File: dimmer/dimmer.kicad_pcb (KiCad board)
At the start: 2 copper layers, 16 parts, among them J1 Conn_01x04, J2 Conn_01x04, Q1 TIC216, U1 4N25, U2 MOC3021M

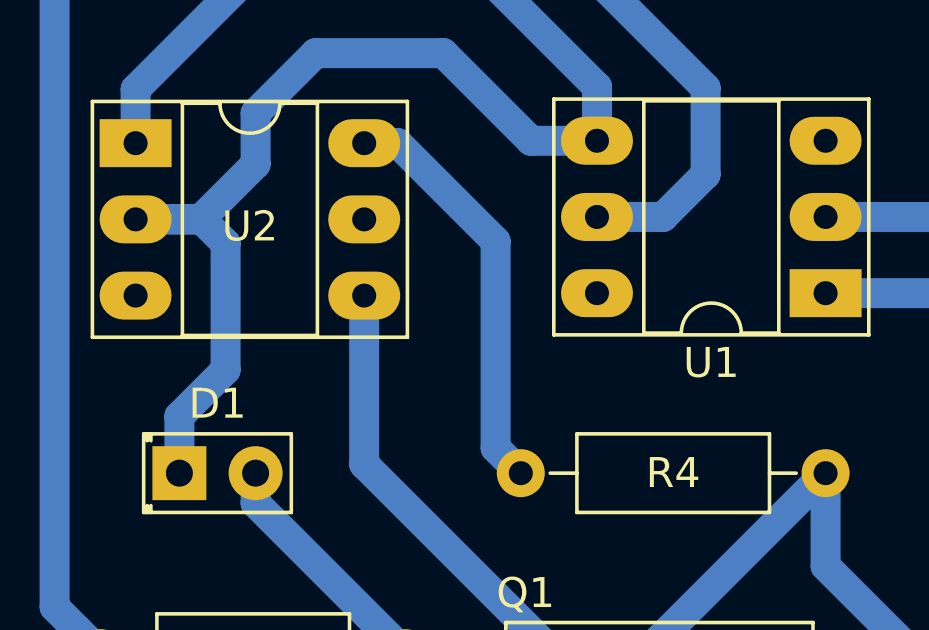
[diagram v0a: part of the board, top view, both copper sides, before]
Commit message: update resistences 1W values
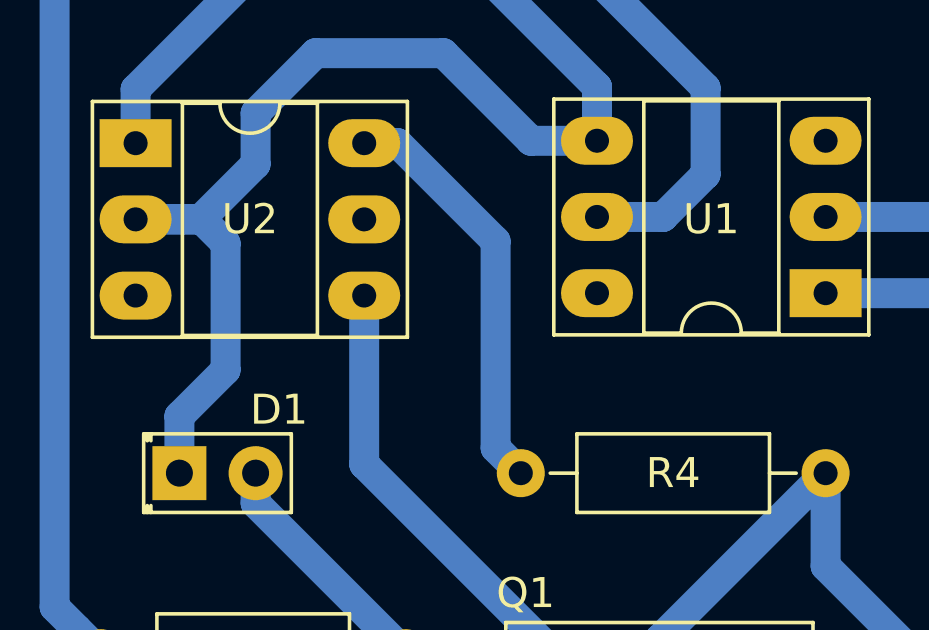
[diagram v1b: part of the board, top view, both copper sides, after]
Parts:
- R5, R6: value 30k/1W -> 15k/1W
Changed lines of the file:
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@@
     (visible_elements FFFFFF7F)
     (pcbplotparams
-      (layerselection 0x010fc_ffffffff)
+      (layerselection 0x3ffff_ffffffff)
       (usegerberextensions false)
       (usegerberattributes false)
@@
       (excludeedgelayer true)
       (linewidth 0.100000)
-      (plotframeref false)
+      (plotframeref true)
       (viasonmask false)
       (mode 1)
@@
       (padsonsilk false)
       (subtractmaskfromsilk false)
-      (outputformat 1)
-      (mirror false)
-      (drillshape 1)
+      (outputformat 4)
+      (mirror true)
+      (drillshape 0)
       (scaleselection 1)
-      (outputdirectory ""))
+      (outputdirectory "plot/"))
   )
   (net 0 "")
@@
     (descr "6-lead though-hole mounted DIP package, row spacing 7.62 mm (300 mils), Socket, LongPads")
     (tags "THT DIP DIL PDIP 2.54mm 7.62mm 300mil Socket LongPads")
-    (fp_text reference U2 (at 3.81 2.78) (layer F.SilkS)
+    (fp_text reference U2 (at 3.81 2.538) (layer F.SilkS)
       (effects (font (size 1 1) (thickness 0.15)))
     )
@@
     (descr "6-lead though-hole mounted DIP package, row spacing 7.62 mm (300 mils), Socket, LongPads")
     (tags "THT DIP DIL PDIP 2.54mm 7.62mm 300mil Socket LongPads")
-    (fp_text reference U1 (at 3.81 -2.33 180) (layer F.SilkS)
+    (fp_text reference U1 (at 3.81 2.462 180) (layer F.SilkS)
       (effects (font (size 1 1) (thickness 0.15)))
     )
@@
     (descr "LED, Round, FlatTop,  Rectangular size 4.8x2.5mm^2 diameter 2.0mm, 2 pins, http://www.kingbright.com/attachments/file/psearch/000/00/00/L-13GD(Ver.11B).pdf")
     (tags "LED Round FlatTop  Rectangular size 4.8x2.5mm^2 diameter 2.0mm 2 pins")
-    (fp_text reference D1 (at 1.27 -2.31) (layer F.SilkS)
+    (fp_text reference D1 (at 3.322 -2.112) (layer F.SilkS)
       (effects (font (size 1 1) (thickness 0.15)))
     )
@@
       (effects (font (size 1 1) (thickness 0.15)))
     )
-    (fp_text value 30k/1W (at 12.8 -1.7 180) (layer F.Fab)
+    (fp_text value 15k/1W (at 12.8 -1.7 180) (layer F.Fab)
       (effects (font (size 1 1) (thickness 0.15)))
     )
@@
       (effects (font (size 1 1) (thickness 0.15)))
     )
-    (fp_text value 30k/1W (at 13.1 -1.68 180) (layer F.Fab)
-      (effects (font (size 1 1) (thickness 0.15)))
-    )
+    (fp_text value 15k/1W (at 13.1 -1.68 180) (layer F.Fab)
+      (effects (font (size 1 1) (thickness 0.15)))
+    )

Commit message: Update dimmer.kicad_pcb
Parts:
- R5, R6: footprint Resistors_THT:R_Axial_DIN0516_L15.5mm_D5.0mm_P25.40mm_Horizontal -> Resistor_THT:R_Axial_DIN0309_L9.0mm_D3.2mm_P12.70mm_Horizontal
- moved U1 42.4 mm to (148.0, 87.1)
- moved D1 39.1 mm to (122.0, 105.5), turned to 270 degrees
- moved R1 37.9 mm to (134.0, 82.0)
- moved R2 37.4 mm to (128.0, 102.0), turned to 270 degrees
- moved R5 35.8 mm to (168.0, 88.0)
- moved R6 35.5 mm to (168.0, 81.0)
- moved J1 35.3 mm to (122.0, 85.0)
- moved J2 35.0 mm to (178.0, 90.0)
- moved D2 32.2 mm to (157.6, 100.4)
- moved D3 32.2 mm to (167.5, 111.6)
- moved D4 32.2 mm to (157.5, 106.0)
- moved D5 32.2 mm to (167.8, 95.0)
- moved Q1 32.2 mm to (148.0, 113.0)
- moved R4 32.2 mm to (151.0, 106.0)
- moved R3 29.1 mm to (134.0, 102.0), turned to 270 degrees
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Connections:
- J1 pad 2: dimmer -> zero-c
- J1 pad 3: zero-c -> dimmer
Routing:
- net GND: track 51.6 -> 71.1 mm
- net Net-(D2-Pad1): track 12.4 -> 23.0 mm
- net dimmer: track 41.7 -> 31.8 mm
- net Net-(D4-Pad2): track 44.2 -> 35.0 mm
- net Net-(D2-Pad2): track 42.5 -> 34.0 mm
- net Net-(D3-Pad2): track 27.2 -> 35.3 mm
- net VAC: track 67.9 -> 75.2 mm
- net Net-(J2-Pad4): track 34.2 -> 39.5 mm
- net zero-c: track 30.1 -> 25.5 mm
- net VCC: track 16.6 -> 13.2 mm
- net Net-(R4-Pad2): track 13.8 -> 16.5 mm
- net NEUT: track 34.1 -> 32.5 mm
- net Net-(R3-Pad1): track 10.9 -> 12.2 mm

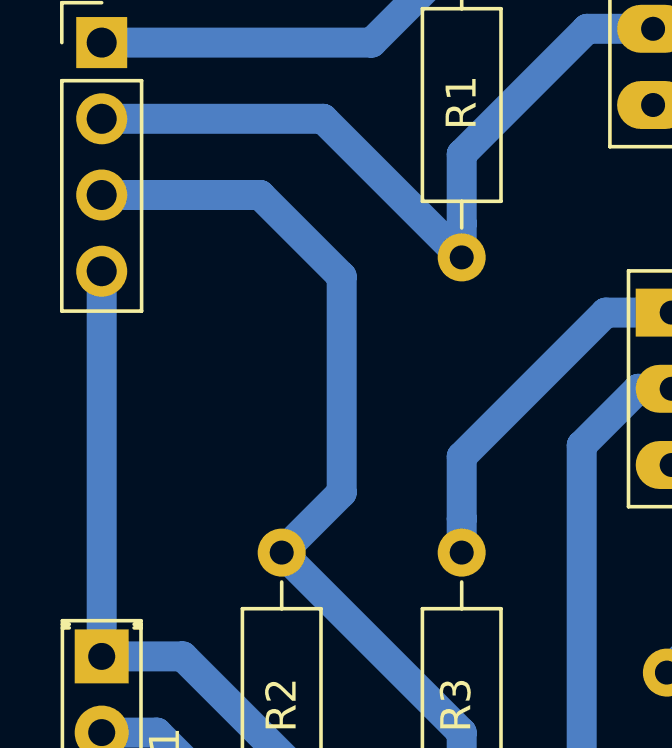
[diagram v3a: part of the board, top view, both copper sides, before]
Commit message: upated dimmer track
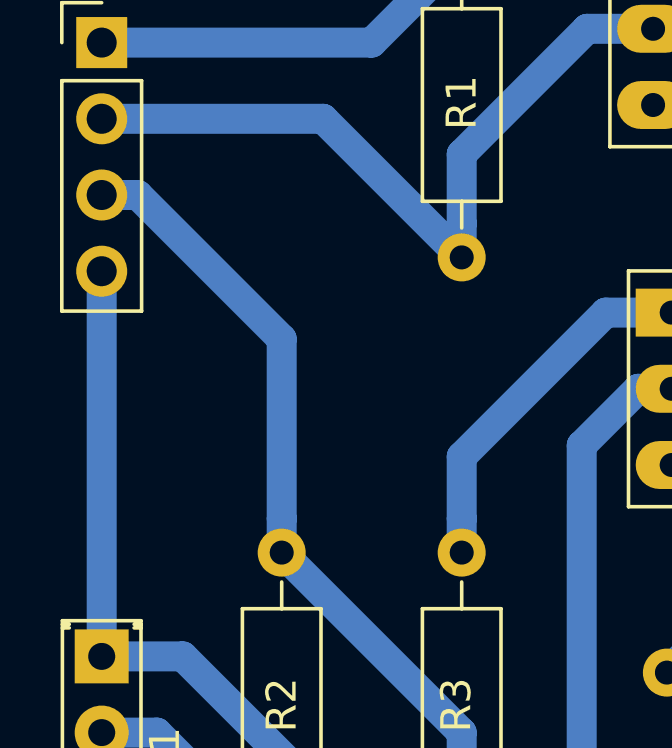
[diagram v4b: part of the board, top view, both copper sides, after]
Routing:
- net dimmer: track 31.8 -> 27.8 mm
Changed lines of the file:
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@@
   (segment (start 134 108) (end 128 102) (width 1) (layer B.Cu) (net 9))
   (segment (start 134 112.16) (end 134 108) (width 1) (layer B.Cu) (net 9))
-  (segment (start 130 100) (end 128 102) (width 1) (layer B.Cu) (net 9))
-  (segment (start 130 92.797919) (end 130 100) (width 1) (layer B.Cu) (net 9))
-  (segment (start 127.282081 90.08) (end 130 92.797919) (width 1) (layer B.Cu) (net 9))
-  (segment (start 122 90.08) (end 127.282081 90.08) (width 1) (layer B.Cu) (net 9))
+  (segment (start 128 100.86863) (end 128 102) (width 1) (layer B.Cu) (net 9))
+  (segment (start 128 94.877919) (end 128 100.86863) (width 1) (layer B.Cu) (net 9))
+  (segment (start 123.202081 90.08) (end 128 94.877919) (width 1) (layer B.Cu) (net 9))
+  (segment (start 122 90.08) (end 123.202081 90.08) (width 1) (layer B.Cu) (net 9))
   (segment (start 128.16 112.16) (end 128 112) (width 1) (layer B.Cu) (net 10))
   (segment (start 123.84 108) (end 128 112.16) (width 1) (layer B.Cu) (net 10))
